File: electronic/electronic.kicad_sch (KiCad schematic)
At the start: 79 parts, among them J1 M_BAT01, J10 BMP01, J11 MPU6050_01, J12 NEO_06_01, J13 CONN, J14 OLED, J15 HCSR01, J16 HCSR02, J17 HCSR03, J18 HCSR04, J19 BAT, J2 M_SIG01, J20 25.5-24 ESP32, J3 M_SIG02, J4 M_BAT02, J5 M_SIG03, J6 M_BAT03, J7 M_SIG04, J8 M_BAT04, J9 DHT01, M1 A2212 KV2200, M2 A2212 KV2200, M3 A2212 KV2200, M4 A2212 KV2200, U1 30A ESC, U10 DEVKIT_V1_ESP32-WROOM-32, U11 RT9193-33GB, U12 CAT24C256, U13 SSD1306, U14 L7805, U15 HC-SR04, U16 HC-SR04, U17 HC-SR04, U18 HC-SR04, U2 30A ESC, U3 30A ESC, U4 30A ESC, U5 BMP280, U6 DHT22, U7 AP2112K-1.2, U8 NEO-6M-GPS, U9 MPU-6050

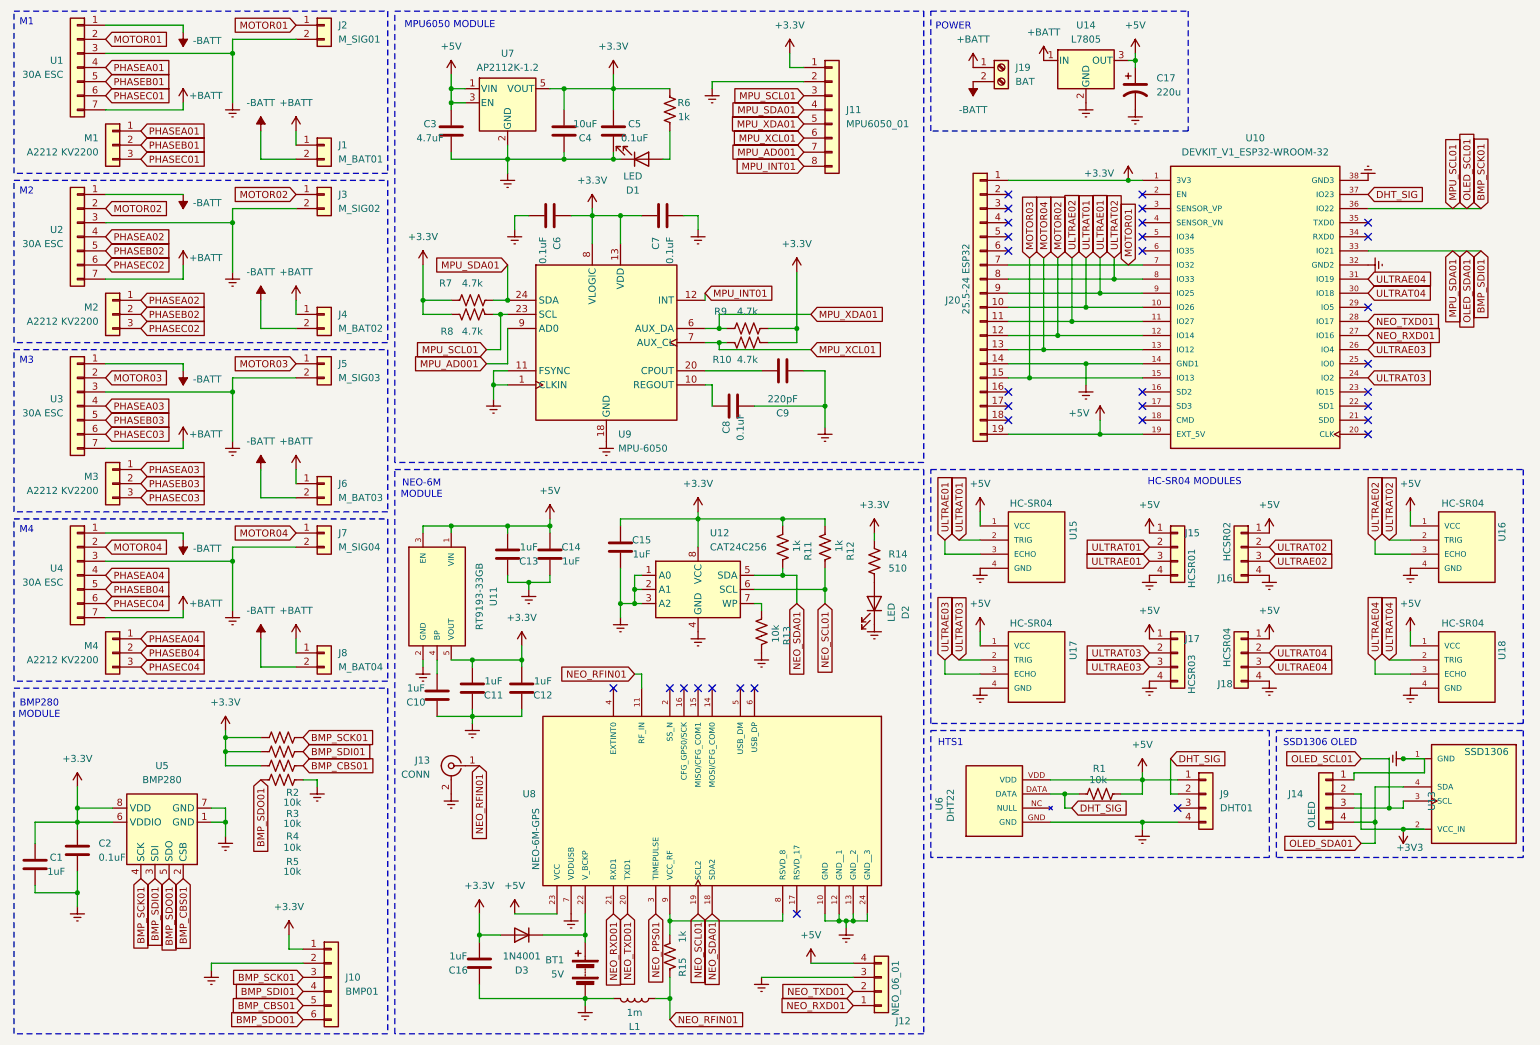
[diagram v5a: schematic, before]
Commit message: refactor (electronic, power): separate the project PCB in two
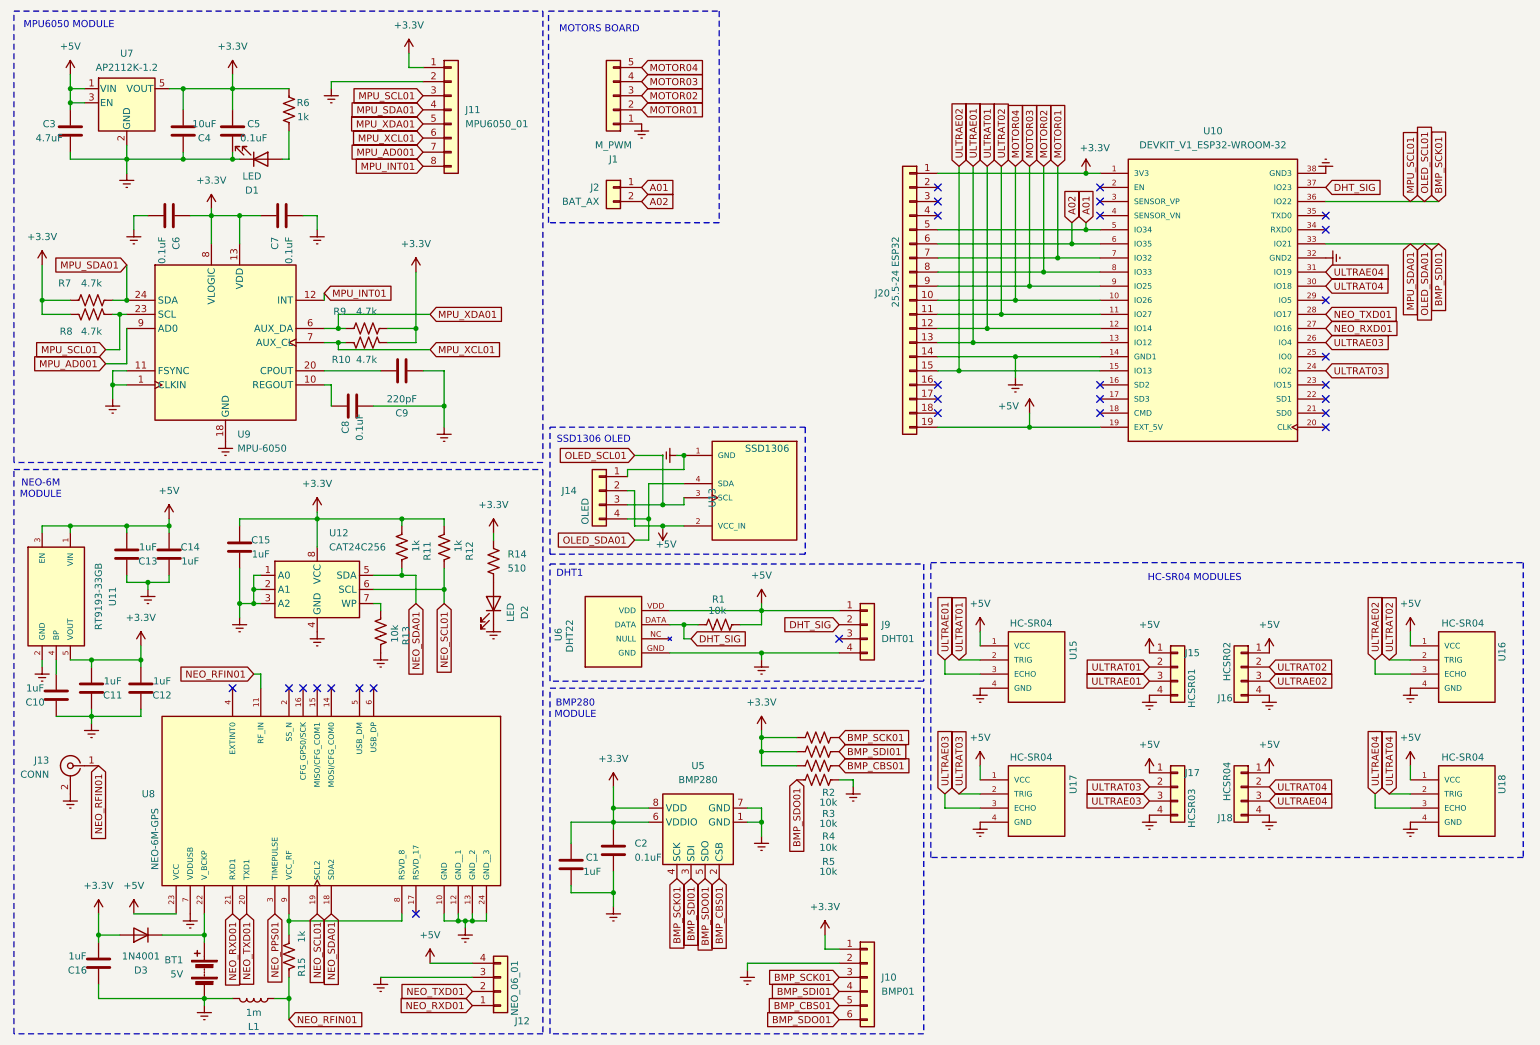
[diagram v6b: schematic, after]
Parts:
- removed C17: 220u, Capacitor_THT:C_Radial_D8.0mm_H11.5mm_P3.50mm, symbol Device:C_Polarized_US
- removed J1: M_BAT01, Connector_JST:JST_XH_B2B-XH-A_1x02_P2.50mm_Vertical, symbol Connector_Generic:Conn_01x02
- removed J19: BAT, custom:DG301-5.0-2P-1X, symbol Connector:Screw_Terminal_01x02
- removed J3: M_SIG02, Connector_JST:JST_XH_B2B-XH-A_1x02_P2.50mm_Vertical, symbol Connector_Generic:Conn_01x02
- removed J4: M_BAT02, Connector_JST:JST_XH_B2B-XH-A_1x02_P2.50mm_Vertical, symbol Connector_Generic:Conn_01x02
- removed J5: M_SIG03, Connector_JST:JST_XH_B2B-XH-A_1x02_P2.50mm_Vertical, symbol Connector_Generic:Conn_01x02
- removed J6: M_BAT03, Connector_JST:JST_XH_B2B-XH-A_1x02_P2.50mm_Vertical, symbol Connector_Generic:Conn_01x02
- removed J7: M_SIG04, Connector_JST:JST_XH_B2B-XH-A_1x02_P2.50mm_Vertical, symbol Connector_Generic:Conn_01x02
- removed J8: M_BAT04, Connector_JST:JST_XH_B2B-XH-A_1x02_P2.50mm_Vertical, symbol Connector_Generic:Conn_01x02
- removed M1, M2, M3, M4: A2212 KV2200, symbol Connector_Generic:Conn_01x03
- removed U1, U2, U3, U4: 30A ESC, symbol Connector_Generic:Conn_01x07
- removed U14: L7805, Package_TO_SOT_SMD:TO-252-2, symbol Regulator_Linear:L7805
- added J1: M_PWM, Connector_JST:JST_XH_B5B-XH-A_1x05_P2.50mm_Vertical, symbol Connector_Generic:Conn_01x05
- J2: value M_SIG01 -> BAT_AX
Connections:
- net +3V3 is gone; now on net +5V: J14.2 (Pin_2), U13.2 (VCC_IN)
- net Earth: now also J1.1 (Pin_1); no longer J2.2 (Pin_2)
- net MOTOR01: now also J1.2 (Pin_2); no longer J2.1 (Pin_1)
- net MOTOR02: now also J20.8 (Pin_8), U10.8 (IO33), J1.3 (Pin_3); no longer J20.12 (Pin_12), U10.12 (IO14)
- net MOTOR03: now also J20.9 (Pin_9), U10.9 (IO25), J1.4 (Pin_4); no longer J20.15 (Pin_15), U10.15 (IO13)
- net MOTOR04: now also J20.10 (Pin_10), U10.10 (IO26), J1.5 (Pin_5); no longer J20.13 (Pin_13), U10.13 (IO12)
- net ULTRAE01: now also J20.13 (Pin_13), U10.13 (IO12); no longer J20.9 (Pin_9), U10.9 (IO25)
- net ULTRAE02: now also J20.15 (Pin_15), U10.15 (IO13); no longer J20.11 (Pin_11), U10.11 (IO27)
- net ULTRAT01: now also J20.12 (Pin_12), U10.12 (IO14); no longer J20.10 (Pin_10), U10.10 (IO26)
- net ULTRAT02: now also J20.11 (Pin_11), U10.11 (IO27); no longer J20.8 (Pin_8), U10.8 (IO33)
- net A01: now reaches J20.5 (Pin_5)
- net A01: now also J2.1 (Pin_1), U10.5 (IO34)
- net A02: now reaches J20.6 (Pin_6)
- net A02: now also J2.2 (Pin_2), U10.6 (IO35)
- no-connect marks 33 -> 29
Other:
- note added: "DHT1"
- note added: "MOTORS BOARD"
- note removed: "HTS1"
- note removed: "M1"
- note removed: "M2"
- note removed: "M3"
- note removed: "M4"
- note removed: "POWER"
- moved on the sheet: BT1, C1, C10, C11, C12, C13, C14, C15, C16, C2, C3, C4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
